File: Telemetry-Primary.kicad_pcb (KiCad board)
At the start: 2 copper layers, 55.9 x 74.9 mm, 45 parts, among them J2 Conn_01x02, J3 Micro_SD_Card_Det, J4 Conn_01x04, J5 Conn_01x04, J6 Conn_02x08_Odd_Even, J7 Conn_02x15_Odd_Even, J8 Conn_02x10_Odd_Even, J9 Conn_02x17_Odd_Even, U2 ADM3055E, U3 PQMC3-Dx-Sx-S, U4 CDSOT23-T24CAN

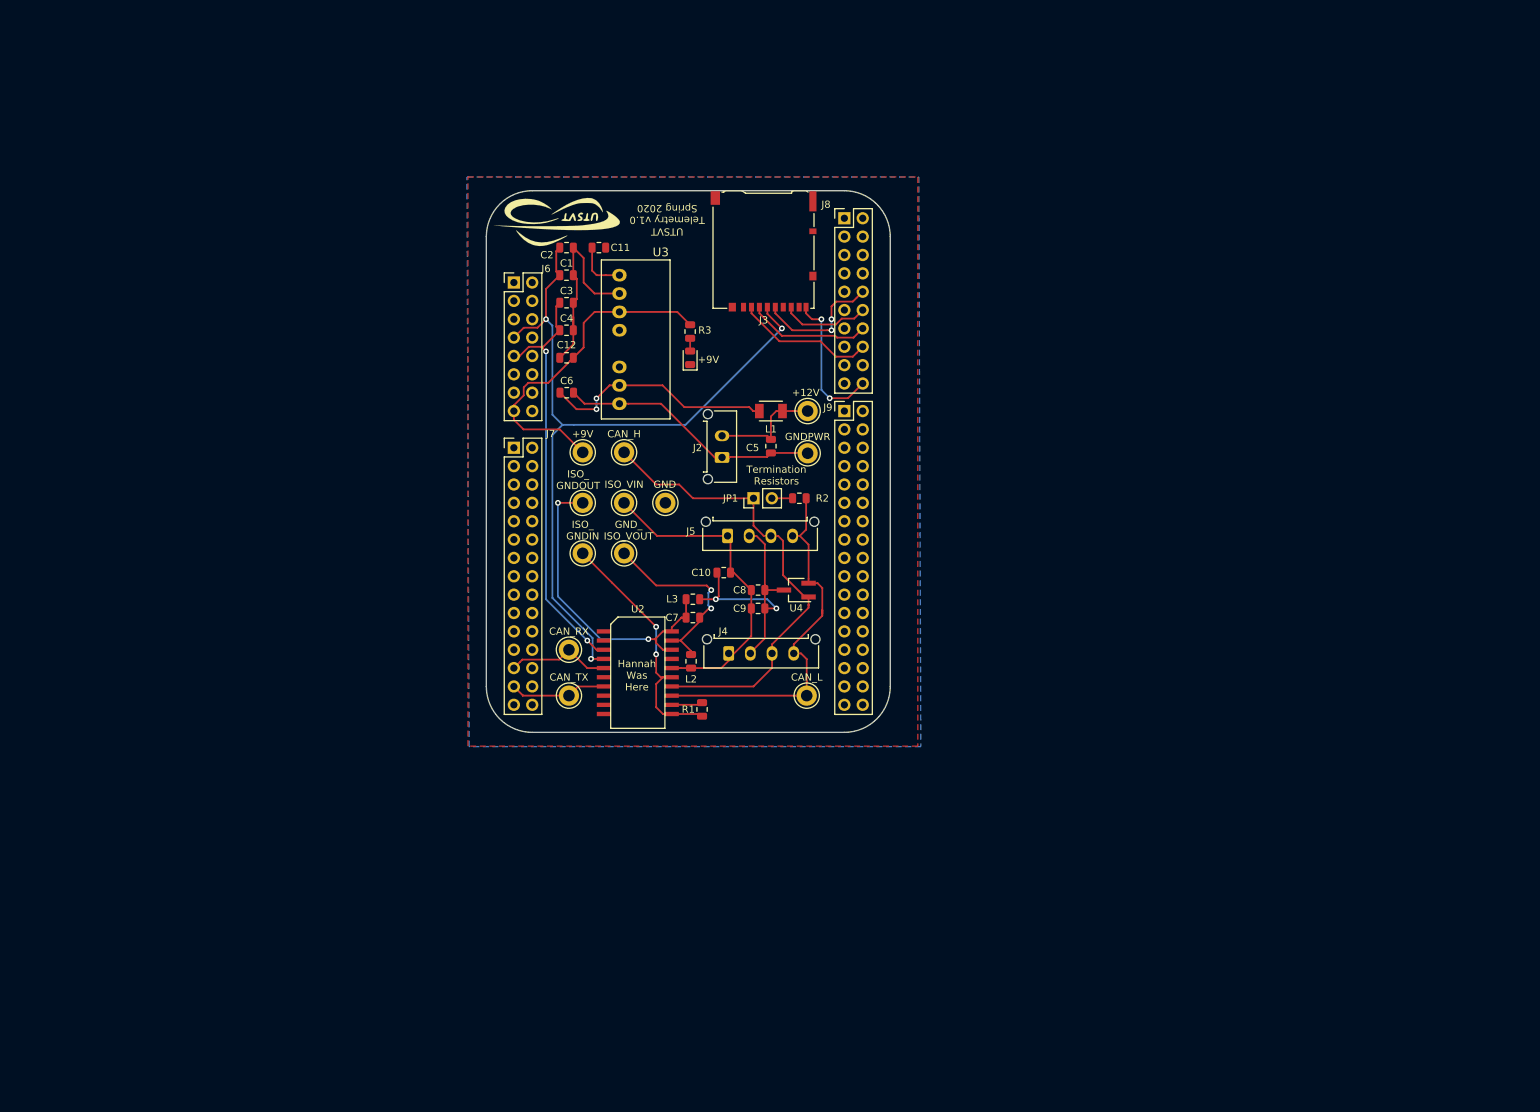
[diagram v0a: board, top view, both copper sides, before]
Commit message: Initial layout of the Telemtry board.
The ethernet interface needs more work.
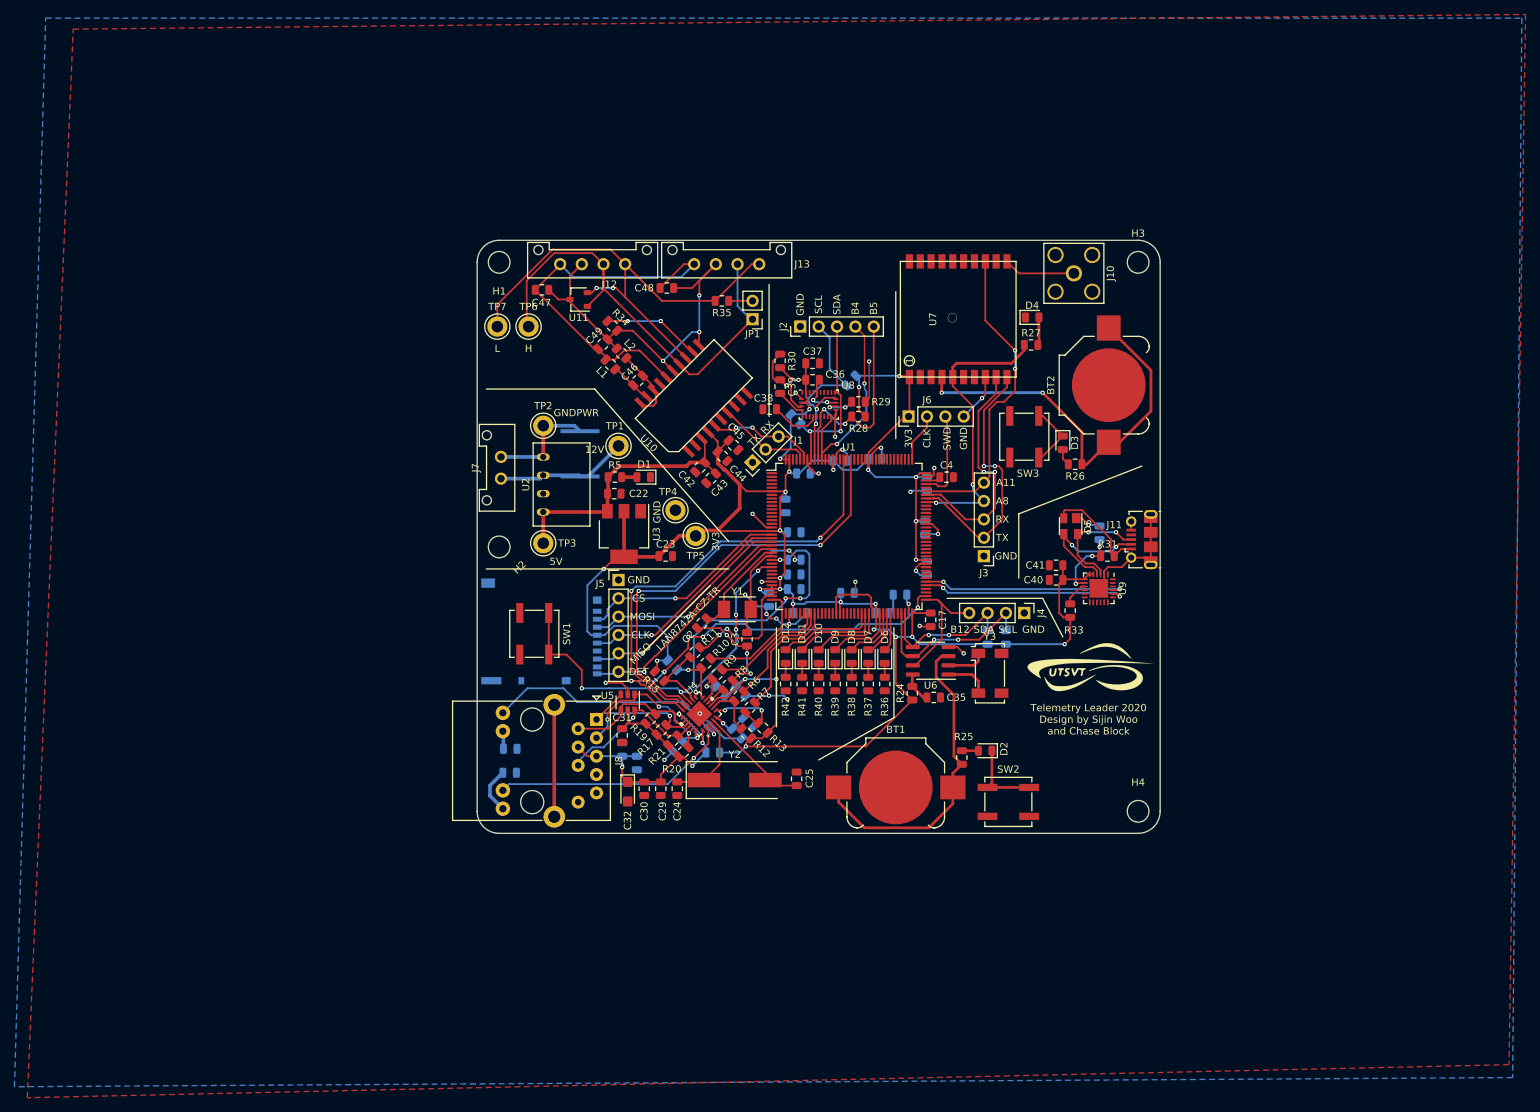
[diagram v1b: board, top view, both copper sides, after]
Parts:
- removed G***: LOGO, UTSVT_Special:Hallock_Image_Small
- removed G***: LOGO, UTSVT_Special:UTSVT_Logo_Symbol
- removed L3: 2k, Inductor_SMD:L_0805_2012Metric
- removed TP10: CAN_L, TestPoint:TestPoint_Keystone_5005-5009_Compact
- removed TP13: 9VIN, TestPoint:TestPoint_Keystone_5005-5009_Compact
- removed TP14: 9V_GND, TestPoint:TestPoint_Keystone_5005-5009_Compact
- removed TP8: CAN_ISO_GNDOUT, TestPoint:TestPoint_Keystone_5005-5009_Compact
- removed TP9: CAN_H, TestPoint:TestPoint_Keystone_5005-5009_Compact
- added BT1: CR1220, Battery:BatteryHolder_Keystone_3000_1x12mm, F.Cu at (129.0, 120.7)
- added BT2: CR1220, Battery:BatteryHolder_Keystone_3000_1x12mm, F.Cu at (158.5, 65.0)
- added C13: 0.1u, Capacitor_SMD:C_0805_2012Metric, B.Cu at (126.2, 75.2)
- added C14: 0.1u, Capacitor_SMD:C_0805_2012Metric, B.Cu at (133.3, 78.7)
- added C15: 0.1u, Capacitor_SMD:C_0805_2012Metric, B.Cu at (133.1, 84.8)
- added C16: 0.1u, Capacitor_SMD:C_0805_2012Metric, B.Cu at (133.3, 90.3)
- added C17: 0.1u, Capacitor_SMD:C_0805_2012Metric, F.Cu at (133.9, 97.5)
- added C18: 0.1u, Capacitor_SMD:C_0805_2012Metric, B.Cu at (127.2, 96.5)
- added C19: 0.1u, Capacitor_SMD:C_0805_2012Metric, B.Cu at (122.3, 93.7)
- added C20: 4.7u, Capacitor_SMD:C_0805_2012Metric, B.Cu at (115.7, 96.5)
- added C21: 10u, UTSVT_Passive:C_2220_5750Metric, B.Cu at (85.3, 74.5)
- added C22: 10u, Capacitor_SMD:C_0805_2012Metric, F.Cu at (90.1, 80.0)
- added C23: 10u, Capacitor_SMD:C_0805_2012Metric, F.Cu at (97.2, 88.6)
- added C24: 30p, Capacitor_SMD:C_0805_2012Metric, F.Cu at (98.8, 120.8)
- added C25: 30p, Capacitor_SMD:C_0805_2012Metric, F.Cu at (115.3, 119.5)
- added C26: 470p, Capacitor_SMD:C_0805_2012Metric, B.Cu at (107.1, 113.2)
- added C27: 1u, Capacitor_SMD:C_0805_2012Metric, B.Cu at (108.6, 111.7)
- added C28: 0.1u, Capacitor_SMD:C_0805_2012Metric, B.Cu at (107.6, 107.3)
- added C29: 0.1u, Capacitor_SMD:C_0805_2012Metric, F.Cu at (96.5, 120.8)
- added C30: 0.1u, Capacitor_SMD:C_0805_2012Metric, F.Cu at (94.2, 120.8)
- added C31: 0.1u, Capacitor_SMD:C_0805_2012Metric, F.Cu at (91.2, 113.5)
- added C32: 10u, Capacitor_Tantalum_SMD:CP_EIA-3216-18_Kemet-A, F.Cu at (91.9, 121.2)
- added C33: 0.1u, Capacitor_SMD:C_0805_2012Metric, B.Cu at (91.2, 115.4)
- added C34: 0.1u, Capacitor_SMD:C_0805_2012Metric, B.Cu at (93.2, 117.3)
- added C35: 10u, Capacitor_SMD:C_0805_2012Metric, F.Cu at (134.3, 108.2)
- added C36: 6.8n, Capacitor_SMD:C_0805_2012Metric, F.Cu at (117.5, 64.3)
- added C37: 120n, Capacitor_SMD:C_0805_2012Metric, F.Cu at (117.5, 62.0)
- added C38: 0.1u, Capacitor_SMD:C_0805_2012Metric, F.Cu at (111.6, 68.3)
- added C39: 100n, Capacitor_SMD:C_0805_2012Metric, F.Cu at (113.0, 65.2)
- added C40: 4.7u, Capacitor_SMD:C_0805_2012Metric, F.Cu at (151.2, 91.9)
- added C41: 0.1u, Capacitor_SMD:C_0805_2012Metric, F.Cu at (151.2, 89.9)
- added C42: 10u, Capacitor_SMD:C_0805_2012Metric, F.Cu at (102.0, 76.4)
- added C43: 0.1u, Capacitor_SMD:C_0805_2012Metric, F.Cu at (103.5, 77.9)
- added C44: 0.1u, Capacitor_SMD:C_0805_2012Metric, F.Cu at (105.1, 74.8)
- added C45: 0.01u, Capacitor_SMD:C_0805_2012Metric, F.Cu at (106.6, 73.3)
- added C46: 0.22u, Capacitor_SMD:C_0805_2012Metric, F.Cu at (93.4, 64.4)
- added C47: 10u, Capacitor_SMD:C_0805_2012Metric, F.Cu at (80.1, 51.8)
- added C48: 0.1u, Capacitor_SMD:C_0805_2012Metric, F.Cu at (97.4, 51.6)
- added C49: 0.01u, Capacitor_SMD:C_0805_2012Metric, F.Cu at (88.5, 59.3)
- added D10: Dashboard, LED_SMD:LED_0805_2012Metric, F.Cu at (118.4, 102.5)
- added D11: BPS, LED_SMD:LED_0805_2012Metric, F.Cu at (116.1, 102.5)
- added D12: Heartbeat, LED_SMD:LED_0805_2012Metric, F.Cu at (113.8, 102.5)
- added D2: RTCC_BattCheck, LED_SMD:LED_0805_2012Metric, F.Cu at (141.4, 115.6)
- added D3: GPS_BattCheck, LED_SMD:LED_0805_2012Metric, F.Cu at (152.1, 73.0)
- added D4: GPS_FIX, LED_SMD:LED_0805_2012Metric, F.Cu at (147.9, 55.6)
- added D5: SP0503BAHTG, Package_TO_SOT_SMD:SOT-143, F.Cu at (153.2, 84.5)
- added D6: RTDArray, LED_SMD:LED_0805_2012Metric, F.Cu at (127.5, 102.5)
- added D7: MPPT1, LED_SMD:LED_0805_2012Metric, F.Cu at (125.2, 102.5)
- added D8: MPPT0, LED_SMD:LED_0805_2012Metric, F.Cu at (122.9, 102.5)
- added D9: Motor, LED_SMD:LED_0805_2012Metric, F.Cu at (120.7, 102.5)
- added FB1: 600, Inductor_SMD:L_0805_2012Metric, B.Cu at (103.7, 115.8)
- added H1: M.3, MountingHole:MountingHole_3mm, F.Cu at (74.2, 48.0)
- added H2: M.3, MountingHole:MountingHole_3mm, F.Cu at (74.2, 87.4)
- added H3: M.3, MountingHole:MountingHole_3mm, F.Cu at (162.6, 48.0)
- added H4: M.3, MountingHole:MountingHole_3mm, F.Cu at (162.6, 124.0)
- added J1: CAN_LogicAnalyzer, Connector_PinHeader_2.54mm:PinHeader_1x03_P2.54mm_Vertical, F.Cu at (109.2, 75.7)
- added J10: SMAConn, Connector_Coaxial:SMA_Amphenol_132203-12_Horizontal, F.Cu at (153.7, 49.5)
- added J11: USB_B_Micro, Connector_USB:USB_Micro-B_Molex-105017-0001, F.Cu at (163.1, 86.4)
- added J12: CAN_In, UTSVT_Connectors:Molex_MicroFit3.0_1x4xP3.00mm_PolarizingPeg_Vertical, F.Cu at (82.6, 48.3)
- added J13: CAN_Out, UTSVT_Connectors:Molex_MicroFit3.0_1x4xP3.00mm_PolarizingPeg_Vertical, F.Cu at (101.1, 48.3)
- added LOGO1: Dr. Hallock, UTSVT_Special:Hallock_Image, B.Cu at (135.1, 110.2)
- added LOGO2: UTSVT Logo, UTSVT_Special:UTSVT_Logo_Symbol, F.Cu at (155.7, 104.1)
- added R10: 33, Resistor_SMD:R_0805_2012Metric, F.Cu at (102.8, 103.5)
- added R11: 33, Resistor_SMD:R_0805_2012Metric, F.Cu at (101.2, 102.0)
- added R12: 10k, Resistor_SMD:R_0805_2012Metric, F.Cu at (108.4, 113.2)
- added R13: 10k, Resistor_SMD:R_0805_2012Metric, F.Cu at (110.6, 112.4)
- added R14: 1.5k, Resistor_SMD:R_0805_2012Metric, B.Cu at (98.1, 103.7)
- added R15: 10k, Resistor_SMD:R_0805_2012Metric, F.Cu at (96.4, 105.3)
- added R16: 10k, Resistor_SMD:R_0805_2012Metric, B.Cu at (104.8, 107.3)
- added R17: 50, Resistor_SMD:R_0805_2012Metric, F.Cu at (96.6, 112.7)
- added R18: 12.1k, Resistor_SMD:R_0805_2012Metric, B.Cu at (98.9, 115.0)
- added R19: 50, Resistor_SMD:R_0805_2012Metric, F.Cu at (95.1, 111.2)
- added R20: 50, Resistor_SMD:R_0805_2012Metric, F.Cu at (99.7, 115.7)
- added R21: 50, Resistor_SMD:R_0805_2012Metric, F.Cu at (98.2, 114.1)
- added R22: 120, Resistor_SMD:R_0805_2012Metric, B.Cu at (75.6, 118.6)
- added R23: 120, Resistor_SMD:R_0805_2012Metric, B.Cu at (75.7, 115.3)
- added R24: 1k, Resistor_SMD:R_0805_2012Metric, F.Cu at (131.3, 107.6)
- added R25: 550, Resistor_SMD:R_0805_2012Metric, F.Cu at (138.2, 116.5)
- added R26: 550, Resistor_SMD:R_0805_2012Metric, F.Cu at (153.8, 75.9)
- added R27: 750, Resistor_SMD:R_0805_2012Metric, F.Cu at (147.7, 59.4)
- added R28: 10k, Resistor_SMD:R_0805_2012Metric, F.Cu at (123.9, 69.3)
- added R29: 10k, Resistor_SMD:R_0805_2012Metric, F.Cu at (123.9, 67.3)
- added R30: 10k, Resistor_SMD:R_0805_2012Metric, F.Cu at (113.0, 61.6)
- added R31: 22.1k, Resistor_SMD:R_0805_2012Metric, F.Cu at (158.3, 88.6)
- added R32: 47.5k, Resistor_SMD:R_0805_2012Metric, B.Cu at (157.2, 85.4)
- added R33: 1k, Resistor_SMD:R_0805_2012Metric, F.Cu at (153.2, 96.2)
- added R34: 0, Resistor_SMD:R_0805_2012Metric, F.Cu at (89.8, 56.8)
- added R35: 120, Resistor_SMD:R_0805_2012Metric, F.Cu at (105.0, 53.3)
- added R36: 750, Resistor_SMD:R_0805_2012Metric, F.Cu at (127.5, 106.3)
- added R37: 750, Resistor_SMD:R_0805_2012Metric, F.Cu at (125.2, 106.3)
- added R38: 750, Resistor_SMD:R_0805_2012Metric, F.Cu at (122.9, 106.3)
- added R39: 750, Resistor_SMD:R_0805_2012Metric, F.Cu at (120.7, 106.3)
- added R4: 4.7k, Resistor_SMD:R_0805_2012Metric, B.Cu at (141.7, 99.9)
- added R40: 750, Resistor_SMD:R_0805_2012Metric, F.Cu at (118.4, 106.3)
- added R41: 750, Resistor_SMD:R_0805_2012Metric, F.Cu at (116.1, 106.3)
- added R42: 680, Resistor_SMD:R_0805_2012Metric, F.Cu at (113.8, 106.3)
- added R5: 1.5k, Resistor_SMD:R_0805_2012Metric, F.Cu at (90.2, 77.7)
- added R6: 33, Resistor_SMD:R_0805_2012Metric, F.Cu at (107.3, 108.0)
- added R7: 33, Resistor_SMD:R_0805_2012Metric, F.Cu at (108.9, 109.6)
- added R8: 10k, Resistor_SMD:R_0805_2012Metric, F.Cu at (105.8, 106.5)
- added R9: 33, Resistor_SMD:R_0805_2012Metric, F.Cu at (104.3, 105.0)
- added SW1: Reset, Button_Switch_SMD:SW_SPST_B3SL-1002P, F.Cu at (79.0, 99.4)
- added SW2: RTCC_BattCheck, Button_Switch_SMD:SW_SPST_B3SL-1002P, F.Cu at (144.6, 122.7)
- added SW3: GPS_BattCheck, Button_Switch_SMD:SW_SPST_B3SL-1002P, F.Cu at (146.8, 72.1)
- added U1: STM32F429ZITx, Package_QFP:LQFP-144_20x20mm_P0.5mm, F.Cu at (122.6, 85.9)
- added U10: ADM3055E, UTSVT_ICs:SOIC-20W_7.5x15.4mm_Pitch1.27mm, F.Cu at (101.1, 66.8)
- added U11: CDSOT23-T24CAN, Package_TO_SOT_SMD:SOT-23W, F.Cu at (85.2, 53.2)
- added U5: USBLC6-4SC6, Package_TO_SOT_SMD:SOT-23-6, F.Cu at (91.9, 108.9)
- added U6: PCF8523T, Package_SO:SOIC-8_3.9x4.9mm_P1.27mm, F.Cu at (133.9, 103.1)
- added U7: MTK3339, UTSVT_Special:FGPMMOPA6H, F.Cu at (137.7, 55.9)
- added U8: BNO055, Package_LGA:LGA-28_5.2x3.8mm_P0.5mm, F.Cu at (118.4, 67.7)
- added U9: CP2102N-A01-GQFN24, Package_DFN_QFN:QFN-24-1EP_4x4mm_P0.5mm_EP2.6x2.6mm, F.Cu at (157.1, 93.1)
- added Y1: 8M, Crystal:Crystal_SMD_TXC_7A-2Pin_5x3.2mm, F.Cu at (107.1, 96.0)
- added Y2: 25M, Crystal:Crystal_SMD_HC49-SD, F.Cu at (106.7, 119.6)
- added Y3: 32.768k, Crystal:Crystal_SMD_Abracon_ABS25-4Pin_8.0x3.8mm, F.Cu at (142.1, 104.9)
- C1, C9: value .1u -> 0.1u; moved to B.Cu
- C10: value .01u -> 0.1u; moved to B.Cu
- C11: value 10u -> 0.1u; moved to B.Cu
- C12, C5: value 100u -> 0.1u; moved to B.Cu
- C2: value .01u -> 18p
- C3: value 10u -> 18p
- C4: value .1u -> 0.1u
- C6: value 47u -> 0.1u; moved to B.Cu
- C7: value .22u -> 0.1u; moved to B.Cu
- C8: value 10u -> 1u; moved to B.Cu
- D1: value LED -> PowerOn
- J2: value Conn_01x02 -> IMU_LogicAnalyzer; footprint Connector_Molex:Molex_Micro-Fit_3.0_43650-0215_1x02_P3.00mm_Vertical -> Connector_PinHeader_2.54mm:PinHeader_1x05_P2.54mm_Vertical
- J3: value Micro_SD_Card_Det -> GPS_LogicAnalyzer; footprint Connector_Card:microSD_HC_Hirose_DM3AT-SF-PEJM5 -> Connector_PinHeader_2.54mm:PinHeader_1x05_P2.54mm_Vertical
- J4: value Conn_01x04 -> RTCC_LogicAnalyzer; footprint Connector_Molex:Molex_Micro-Fit_3.0_43650-0415_1x04_P3.00mm_Vertical -> Connector_PinHeader_2.54mm:PinHeader_1x04_P2.54mm_Vertical
- J5: value Conn_01x04 -> SDCard_LogicAnalyzer; footprint Connector_Molex:Molex_Micro-Fit_3.0_43650-0415_1x04_P3.00mm_Vertical -> Connector_PinHeader_2.54mm:PinHeader_1x06_P2.54mm_Vertical
- J6: value Conn_02x08_Odd_Even -> SWD; footprint Connector_PinHeader_2.54mm:PinHeader_2x08_P2.54mm_Vertical -> Connector_PinHeader_2.54mm:PinHeader_1x04_P2.54mm_Vertical
- J7: value Conn_02x15_Odd_Even -> PowerConn; footprint Connector_PinHeader_2.54mm:PinHeader_2x15_P2.54mm_Vertical -> UTSVT_Connectors:Molex_MicroFit3.0_1x2xP3.00mm_PolarizingPeg_Vertical
- J8: value Conn_02x10_Odd_Even -> RJ45_Abracon_ARJP11A-MASA-B-A-EMU2; footprint Connector_PinHeader_2.54mm:PinHeader_2x10_P2.54mm_Vertical -> Connector_RJ:RJ45_Abracon_ARJP11A-MA_Horizontal
- J9: value Conn_02x17_Odd_Even -> Micro_SD_Card_Det; footprint Connector_PinHeader_2.54mm:PinHeader_2x17_P2.54mm_Vertical -> Connector_Card:microSD_HC_Hirose_DM3AT-SF-PEJM5; moved to B.Cu
- JP1: value Jumper -> Termination RES
- L1: value 5u -> 2k; footprint Inductor_SMD:L_TDK_NLV32_3.2x2.5mm -> Inductor_SMD:L_0805_2012Metric
- R1: value 0 -> 4.7k; moved to B.Cu
- R2: value 120 -> 4.7k; moved to B.Cu
- R3: value 3k -> 4.7k; moved to B.Cu
- TP1: value CAN_TD -> +12V_TP
- TP2: value CAN_RD -> GNDPWR_TP
- TP3: value 12VIN -> +5V_TP
- TP4: value 12V_GND -> GND_TP
- TP5: value CAN_ISO_VIN -> +3.3V_TP
- TP6: value CAN_ISO_VOUT -> CAN_H
- TP7: value CAN_ISO_GNDIN -> CAN_L
- U2: value ADM3055E -> RI3-1205S; footprint UTSVT_ICs:SOIC-20W_7.5x15.4mm_Pitch1.27mm -> UTSVT_ICs:RI3_DC_Converter
- U3: value PQMC3-Dx-Sx-S -> NCP1117-3.3_SOT223; footprint UTSVT_ICs:CUI_PQMC3-S -> Package_TO_SOT_SMD:SOT-223-3_TabPin2
- U4: value CDSOT23-T24CAN -> LAN8742A-CZ-TR; footprint Package_TO_SOT_SMD:SOT-23W_Handsoldering -> UTSVT_ICs:LAN8742AI-CZ-TR
- moved J8 77.4 mm to (87.6, 111.3), turned to 270 degrees
- moved C1 63.9 mm to (129.6, 94.0), turned to 180 degrees
- moved R3 60.8 mm to (144.3, 99.9), turned to 90 degrees
- moved J6 57.7 mm to (130.8, 69.3), turned to 90 degrees
- moved C4 56.4 mm to (136.1, 77.7)
- moved C2 55.2 mm to (102.2, 97.9), turned to 225 degrees
- moved C3 52.8 mm to (108.5, 100.2), turned to 90 degrees
- moved J3 52.0 mm to (141.2, 88.6)
- moved J9 51.8 mm to (80.0, 99.1), turned to 90 degrees
- moved R1 49.9 mm to (122.8, 64.4), turned to 225 degrees
- moved L2 43.7 mm to (91.1, 60.6), turned to 315 degrees
- moved C11 42.1 mm to (116.3, 77.2)
- moved C6 41.6 mm to (115.0, 93.2)
- moved J4 41.3 mm to (146.8, 96.5), turned to 270 degrees
- moved TP3 40.9 mm to (80.3, 86.9), turned to 90 degrees
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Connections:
- net Net-(J8-Pad15) renamed GND2
- C1 pad 1: +3V3 -> Net-(C1-Pad1)
- C10 pad 1: Net-(C10-Pad1) -> /NRST
- C10 pad 2: Net-(C10-Pad2) -> GND
- C11 pad 1: Net-(C11-Pad1) -> +3V3
- C12 pad 1: +9V -> +3V3
- C2 pad 1: +3V3 -> Net-(C2-Pad1)
- C3 pad 1: +5V -> GND
- C3 pad 2: GND -> Net-(C3-Pad2)
- C4 pad 1: +5V -> Net-(C4-Pad1)
- C5 pad 1: +12V -> +3V3
- C5 pad 2: GNDPWR -> GND
- C6 pad 1: Net-(C6-Pad1) -> +3V3
- C6 pad 2: GNDPWR -> GND
- C7 pad 1: Net-(C7-Pad1) -> +3V3
- C7 pad 2: Net-(C7-Pad2) -> GND
- C8 pad 1: Net-(C10-Pad1) -> +3V3
- C8 pad 2: Net-(C10-Pad2) -> GND
- C9 pad 1: Net-(C10-Pad1) -> +3V3
- C9 pad 2: Net-(C10-Pad2) -> GND
- J2 pad 1: GNDPWR -> GND
- J2 pad 2: +12V -> /I2C1_SCL
- J3 pad 1: Net-(J3-Pad1) -> GND
- J3 pad 2: /CS -> /USART1_TX
- J3 pad 3: /MOSI -> /USART1_RX
- J3 pad 4: +3V3 -> /PA8
- J3 pad 5: /CLOCK -> /PA11
- J4 pad 1: Net-(C10-Pad1) -> GND
- J4 pad 2: Net-(C10-Pad2) -> /I2C2_SCL
- J4 pad 3: Net-(J4-Pad3) -> /I2C2_SDA
- J4 pad 4: Net-(J4-Pad4) -> /PB12
- J5 pad 1: Net-(C10-Pad1) -> GND
- J5 pad 2: Net-(C10-Pad2) -> /SPI5_CS
- J5 pad 3: Net-(J4-Pad3) -> /SPI5_MOSI
- J5 pad 4: Net-(J4-Pad4) -> /SPI5_CLK
- J6 pad 1: Net-(J6-Pad1) -> +3V3
- J6 pad 2: Net-(J6-Pad2) -> /SWCLK
- J6 pad 3: Net-(J6-Pad3) -> /SWDIO
- J6 pad 4: Net-(J6-Pad4) -> GND
- J7 pad 1: Net-(J7-Pad1) -> +12V
- J7 pad 2: Net-(J7-Pad2) -> GNDPWR
- J8 pad 10: /CLOCK -> (no net)
- J8 pad 11: Net-(J8-Pad11) -> /Ethernet/LED1
- J8 pad 12: /MISO -> Net-(J8-Pad12)
- J8 pad 13: Net-(J8-Pad13) -> /Ethernet/LED2
- J8 pad 14: /MOSI -> Net-(J8-Pad14)
- J8 pad 4: Net-(J8-Pad4) -> Net-(C29-Pad2)
- J8 pad 5: Net-(J8-Pad5) -> Net-(C29-Pad2)
- J8 pad 7: Net-(J8-Pad7) -> (no net)
- J8 pad 9: Net-(J8-Pad9) -> (no net)
- J9 pad 1: Net-(J9-Pad1) -> (no net)
- J9 pad 10: Net-(J9-Pad10) -> (no net)
- J9 pad 11: Net-(J9-Pad11) -> GND
- J9 pad 2: Net-(J9-Pad2) -> /SPI5_CS
- J9 pad 3: Net-(J9-Pad3) -> /SPI5_MOSI
- J9 pad 4: Net-(J9-Pad4) -> +3V3
- J9 pad 5: Net-(J9-Pad5) -> /SPI5_CLK
- J9 pad 6: Net-(J9-Pad6) -> GND
- J9 pad 7: Net-(J9-Pad7) -> /SPI5_MISO
- J9 pad 8: Net-(J9-Pad8) -> (no net)
- J9 pad 9: Net-(J9-Pad9) -> /SD_DET
- JP1 pad 1: Net-(J4-Pad3) -> /CAN/CAN_H
- L1 pad 1: +12V -> Net-(C47-Pad1)
- L1 pad 2: Net-(C6-Pad1) -> Net-(C46-Pad1)
- L2 pad 1: Net-(C7-Pad1) -> Net-(C47-Pad2)
- L2 pad 2: Net-(C10-Pad1) -> Net-(C46-Pad2)
- R1 pad 1: Net-(R1-Pad1) -> +3V3
- R1 pad 2: Net-(R1-Pad2) -> /I2C1_SCL
- R2 pad 1: Net-(JP1-Pad2) -> +3V3
- R2 pad 2: Net-(J4-Pad4) -> /I2C1_SDA
- R3 pad 1: +9V -> +3V3
- R3 pad 2: Net-(D1-Pad2) -> /I2C2_SCL
- TP1 pad 1: /CAN_TD -> +12V
- TP2 pad 1: /CAN_RD -> GNDPWR
- TP3 pad 1: +12V -> +5V
- TP4 pad 1: GNDPWR -> GND
- TP5 pad 1: Net-(C10-Pad1) -> +3V3
- TP6 pad 1: Net-(C7-Pad1) -> /CAN/CAN_H
- TP7 pad 1: Net-(R1-Pad1) -> /CAN/CAN_L
- U2 pad 1: GND -> GNDPWR
- U2 pad 2: GND -> +12V
- U2 pad 3: +5V -> GND
- U2 pad 4: +3V3 -> +5V
- U3 pad 1: GNDPWR -> GND
- U3 pad 2: Net-(C6-Pad1) -> +3V3
- U3 pad 3: Net-(U3-Pad3) -> +5V
- U4 pad 1: Net-(J4-Pad3) -> Net-(C29-Pad2)
- U4 pad 2: Net-(J4-Pad4) -> /Ethernet/LED2
- U4 pad 3: Net-(C10-Pad2) -> /Ethernet/LED1
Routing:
- net +3V3: track 108.9 -> 358.6 mm, vias 3 -> 29
- net GND: track 29.8 -> 154.0 mm, vias 0 -> 33
- net /CAN/CAN_L: track 0.00 -> 70.0 mm, vias 0 -> 2
- net /NRST: track 0.00 -> 68.7 mm, vias 0 -> 5
- net /CAN/CAN_H: track 0.00 -> 66.9 mm
- net Net-(J4-Pad3): track 65.8 -> 0.00 mm
- net /RMII_TXD0: track 0.00 -> 62.0 mm, vias 0 -> 2
- net /RMII_TX_EN: track 0.00 -> 61.6 mm, vias 0 -> 2
- net /RMII_TXD1: track 0.00 -> 56.8 mm, vias 0 -> 5
- net Net-(C47-Pad2): track 0.00 -> 56.4 mm, vias 0 -> 3
- net Net-(C47-Pad1): track 0.00 -> 55.5 mm
- net /GPS/GPS_VBAT: track 0.00 -> 54.8 mm, vias 0 -> 2
- net Net-(J4-Pad4): track 53.1 -> 0.00 mm
- net Net-(C29-Pad2): track 0.00 -> 49.1 mm, vias 0 -> 4
- net +9V: track 48.6 -> 0.00 mm
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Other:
- board size 55.9 x 74.9 mm -> 94.5 x 82 mm
- board text added: "12V"
- board text added: "3V3"
- board text added: "5V"
- board text added: "A11"
- board text added: "A8"
- board text added: "B12"
- board text added: "B4"
- board text added: "B5"
- board text added: "CLK"
- board text added: "CS"
- board text added: "DET"
- board text added: "H"
- board text added: "L"
- board text added: "MISO"
- board text added: "MOSI"
- board text added: "RX"
- board text added: "SCL"
- board text added: "SDA"
- board text added: "SWD"
- board text added: "TX"
- board text added: "Telemetry Leader 2020 Design by Sijin Woo and Chase Block"
- board text removed: "+12V"
- board text removed: "+9V"
- board text removed: "CAN_H"
- board text removed: "CAN_L"
- board text removed: "CAN_RX"
- board text removed: "CAN_TX"
- board text removed: "GND_ ISO_VOUT"
- board text removed: "Hannah Was Here"
- board text removed: "ISO_ GNDIN"
- board text removed: "ISO_ GNDOUT"
- board text removed: "ISO_VIN"
- board text removed: "Termination Resistors"
- board text removed: "UTSVT Telemetry v1.0 Spring 2020"

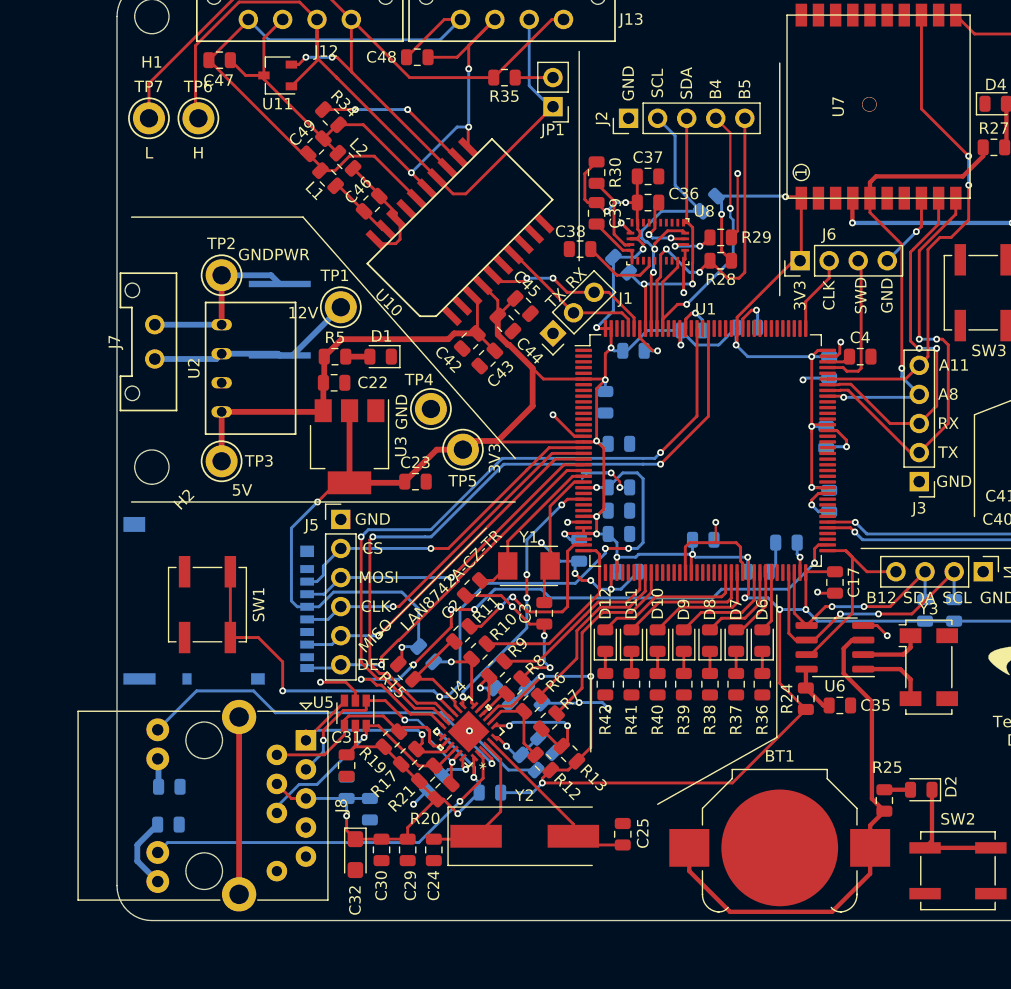
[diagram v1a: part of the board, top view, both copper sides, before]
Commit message: Lay out the Telemetry board.
This is the initial draft of the Telemetry board layout. A few
debugging pins changed (on the SD card) for easier routing.

There is still some uncertainty with regard to the routing of the
Ethernet traces. According to my calculations, the differential
impedence between the RX+/- traces and the TX+/- traces is around
150R, which is 50% higher than one source was recommending. I am
uncertain how to reduce this though, and I am unclear as to how
much this will affect performance, especially when the traces
cover such a short distance.
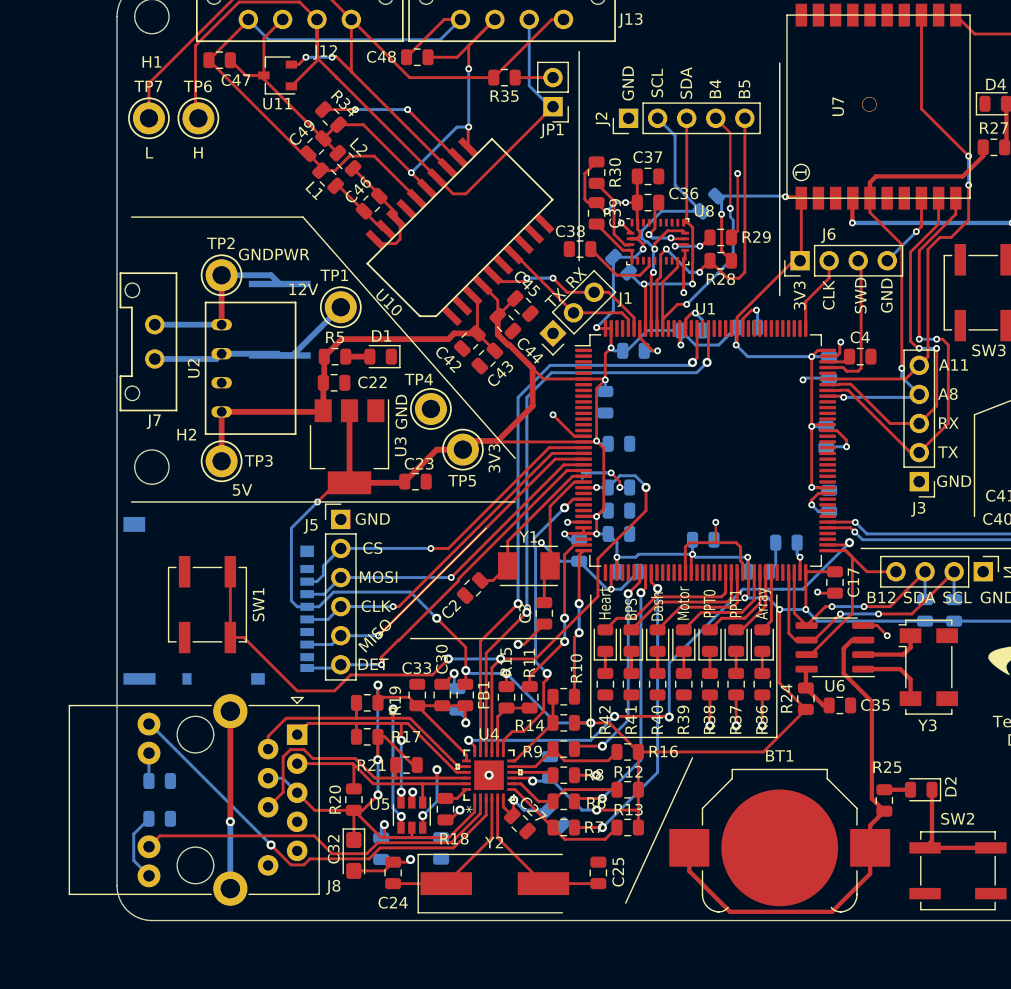
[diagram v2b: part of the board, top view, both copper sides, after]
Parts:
- C27, C33, FB1, R14, R16, R18: moved to F.Cu
- C29, C31: moved to B.Cu
- moved C30 14.5 mm to (99.5, 107.3), turned to 270 degrees
- moved R14 13.4 mm to (110.2, 109.7), turned to 0 degrees
- moved C34 12.3 mm to (100.9, 107.7), turned to 270 degrees
- moved R16 12.0 mm to (115.7, 112.3), turned to 180 degrees
- moved C33 10.2 mm to (97.4, 107.3)
- moved U5 10.2 mm to (96.9, 117.8)
- moved R7 9.39 mm to (110.2, 118.9), turned to 0 degrees
- moved R9 9.14 mm to (110.2, 112.0), turned to 0 degrees
- moved R15 9.07 mm to (105.2, 107.5), turned to 90 degrees
- moved R6 8.99 mm to (110.2, 116.6), turned to 0 degrees
- moved R8 8.90 mm to (110.2, 114.3), turned to 0 degrees
- moved FB1 8.80 mm to (101.5, 107.3), turned to 270 degrees
- moved R10 8.38 mm to (110.2, 107.4), turned to 0 degrees
- moved R13 8.22 mm to (115.7, 118.9), turned to 180 degrees
- moved R11 8.12 mm to (107.2, 107.5), turned to 90 degrees
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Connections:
- net Net-(J8-Pad1) renamed /Ethernet/TX+
- net Net-(J8-Pad2) renamed /Ethernet/TX-
- net Net-(J8-Pad3) renamed /Ethernet/RX+
- net Net-(J8-Pad6) renamed /Ethernet/RX-
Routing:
- net Net-(C29-Pad2): track 49.1 -> 71.5 mm, vias 4 -> 5
- net /Ethernet/TX-: track 19.2 -> 33.7 mm, vias 0 -> 2
- net GND: track 154.0 -> 142.6 mm
- net /RMII_TXD1: track 56.8 -> 46.5 mm, vias 5 -> 4
- net /RMII_TXD0: track 62.0 -> 52.0 mm
- net /RMII_RXD1: track 17.2 -> 27.0 mm, vias 0 -> 2
- net /RMII_TX_EN: track 61.6 -> 52.6 mm
- net /Ethernet/RX-: track 21.5 -> 29.8 mm, vias 1 -> 2
- net /RMII_RXD0: track 16.1 -> 23.8 mm, vias 0 -> 2
- net Net-(R16-Pad2): track 5.88 -> 10.6 mm, vias 1 -> 0
- net Net-(R11-Pad1): track 10.2 -> 6.25 mm
- net /RMII_MDC: track 23.2 -> 27.1 mm, vias 4 -> 2
- net /Ethernet/TX+: track 21.3 -> 25.1 mm, vias 1 -> 2
- net /RMII_MDIO: track 16.6 -> 13.1 mm, vias 0 -> 2
- net /RMII_CRS_DV: track 15.9 -> 19.1 mm, vias 0 -> 2
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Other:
- board text added: "Array"
- board text added: "BPS"
- board text added: "Dash"
- board text added: "Heart"
- board text added: "Motor"
- board text added: "PPT0"
- board text added: "PPT1"
